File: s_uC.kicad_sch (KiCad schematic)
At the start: 18 parts

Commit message: passif en 0402
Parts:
- removed C? (x4): 100nF, Capacitor_SMD:C_0603_1608Metric, symbol Device:C
- removed C? (x2): 20pF, Capacitor_SMD:C_0603_1608Metric, symbol Device:C
- removed R?: 100k, Resistor_SMD:R_0603_1608Metric, symbol Device:R
- added C? (x4): 100nF, Capacitor_SMD:C_0402_1005Metric, symbol Device:C
- added C? (x2): 20pF, Capacitor_SMD:C_0402_1005Metric, symbol Device:C
- added R?: 100k, Resistor_SMD:R_0402_1005Metric, symbol Device:R
- C?: footprint Capacitor_SMD:C_0603_1608Metric -> Capacitor_SMD:C_0402_1005Metric; LCSC C14663 -> C1525
- R?: footprint Resistor_SMD:R_0603_1608Metric -> Resistor_SMD:R_0402_1005Metric; LCSC C25803 -> C25741
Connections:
- net 0V: now also C?.1, C?.1, C?.1, C?.1, C?.1, C?.1
- net 3V3: now also C?.2, C?.2, C?.2, C?.2, R?.1
- net at U?.6 (PD1), Y?.1: now also C?.2
- net at U?.5 (PD0), Y?.2: now also C?.2
- net at C?.2, JP?.1 (A), JP?.1 (A)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: now also R?.2

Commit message: placement
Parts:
- removed JP?: SolderJumper_2_Open, Jumper:SolderJumper-2_P1.3mm_Open_TrianglePad1.0x1.5mm, symbol Jumper:SolderJumper_2_Open
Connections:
- net B0: no longer R?.2, U?.44 (BOOT0)
- net nRST: now also C?.2, JP?.1 (A), R?.2, U?.7 (NRST)
- new net boot: R?.2, U?.44 (BOOT0)

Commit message: routage fini
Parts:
- removed JP? (x6): SolderJumper_2_Open, Jumper:SolderJumper-2_P1.3mm_Open_TrianglePad1.0x1.5mm, symbol Jumper:SolderJumper_2_Open
- added J3: Conn_02x05_Odd_Even, Connector_PinSocket_2.00mm:PinSocket_2x05_P2.00mm_Horizontal, symbol Connector_Generic:Conn_02x05_Odd_Even
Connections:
- net 0V: now also J3.2 (Pin_2)
- net 3V3: now also J3.10 (Pin_10)
- net A13: now also J3.5 (Pin_5)
- net A14: now also J3.7 (Pin_7)
- net A2: now also J3.4 (Pin_4)
- net A3: now also J3.6 (Pin_6)
- net A8: now also J3.9 (Pin_9)
- net nRST: now also J3.8 (Pin_8)
- no-connect marks 0 -> 2
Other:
- note added: "T_CLK"
- note added: "T_DIO"
- note added: "T_RST"
- note added: "T_RX"
- note added: "T_SWO"
- note added: "T_TX"
- note added: "pour être compatible avec le connecteur MIDI du STLINK-V3minie"

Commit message: Passage à kicad 8
et correction des chemins spécifiques
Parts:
- gave numbers to parts that had none: 11

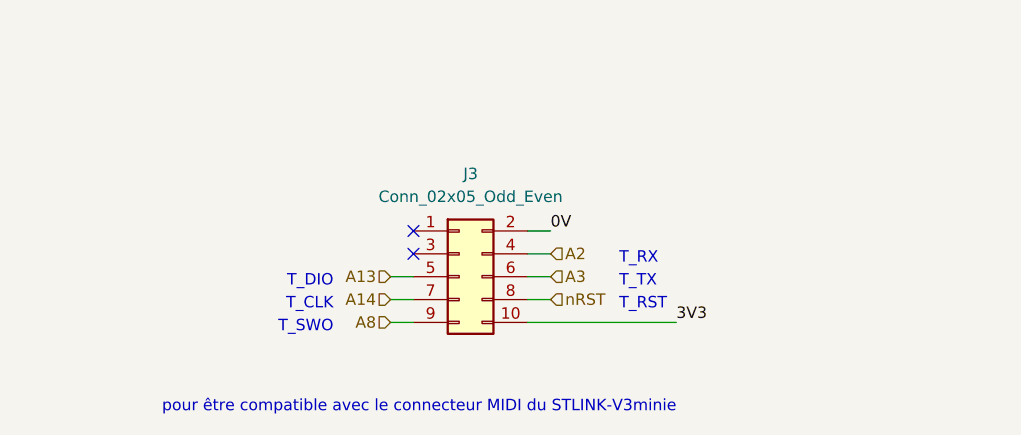
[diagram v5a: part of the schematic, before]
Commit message: Chgt connecteur programmation
passage à 2,54mm
alignement avec grille
silk: ajout pins
maj schéma pour clarification
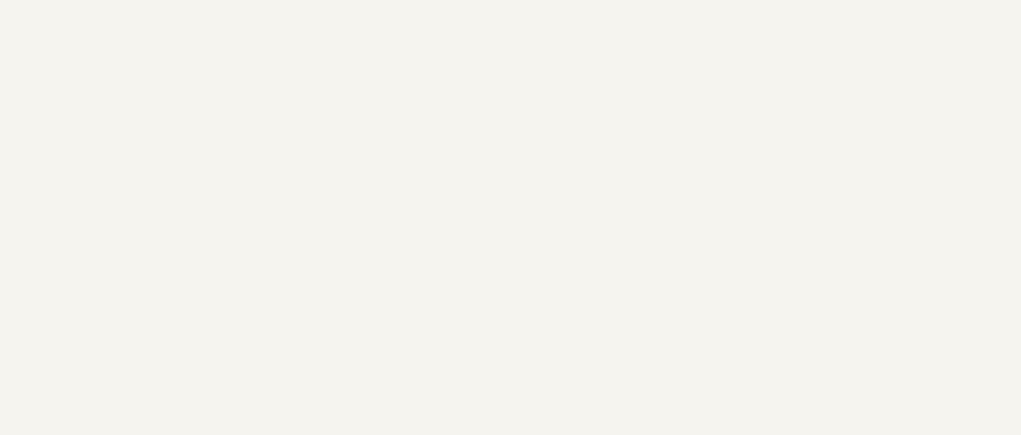
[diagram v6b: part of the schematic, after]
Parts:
- removed J3: Conn_02x05_Odd_Even, Connector_PinSocket_2.00mm:PinSocket_2x05_P2.00mm_Horizontal, symbol Connector_Generic:Conn_02x05_Odd_Even
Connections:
- no-connect marks 2 -> 0
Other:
- note removed: "pour être compatible avec le connecteur MIDI du STLINK-V3minie"

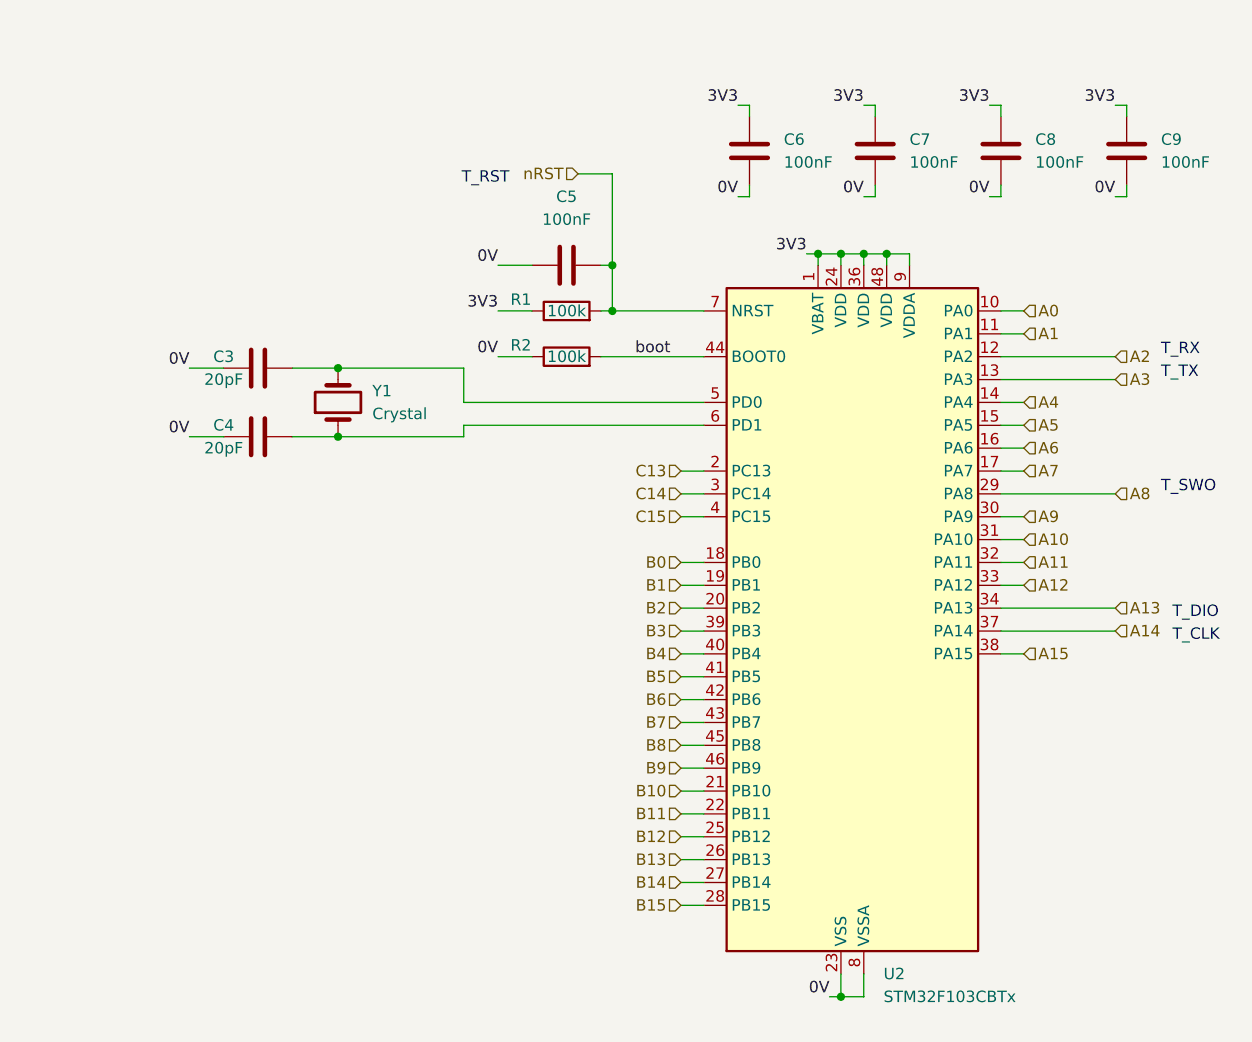
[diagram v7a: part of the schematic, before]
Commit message: changement connecteur prog/debug par ST14
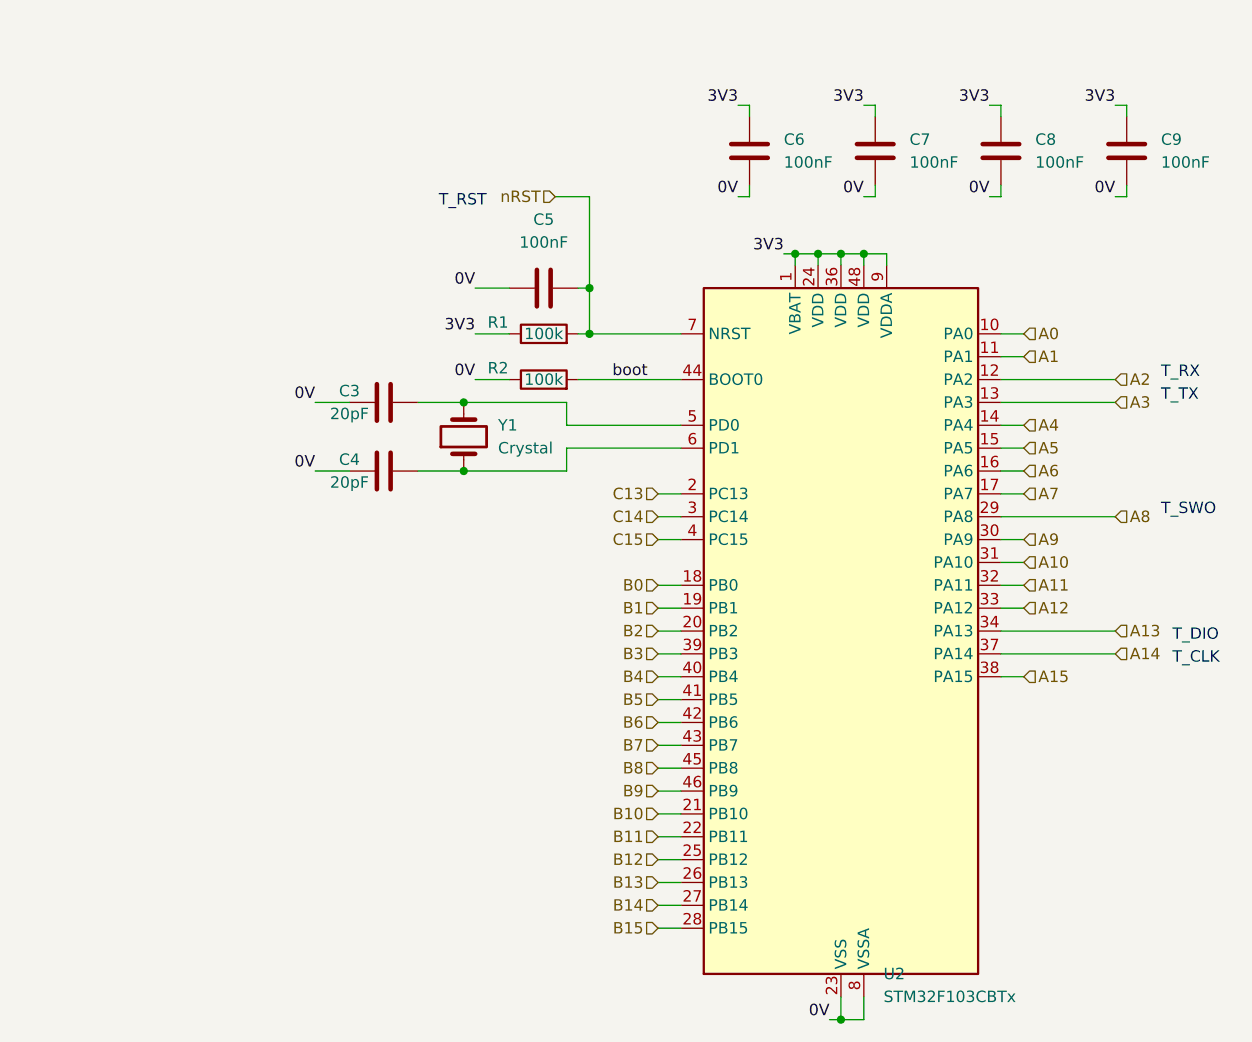
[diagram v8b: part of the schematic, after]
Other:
- moved on the sheet: C3, C4, C5, R1, R2, U2, Y1
